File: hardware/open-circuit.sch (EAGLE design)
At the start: 72 parts, among them IC1 PIC16F1825SO14, IC2 74HC595D, IC3 MCP4728_QUAD_DAC, IC4 LM324D, IC6 LM27675M5_CHARGEPUMP

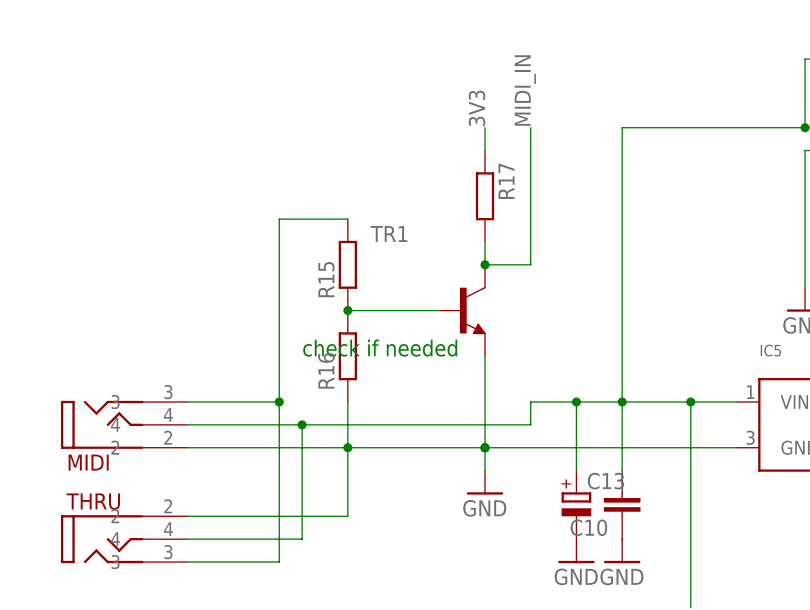
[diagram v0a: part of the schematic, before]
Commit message: fix input transistor
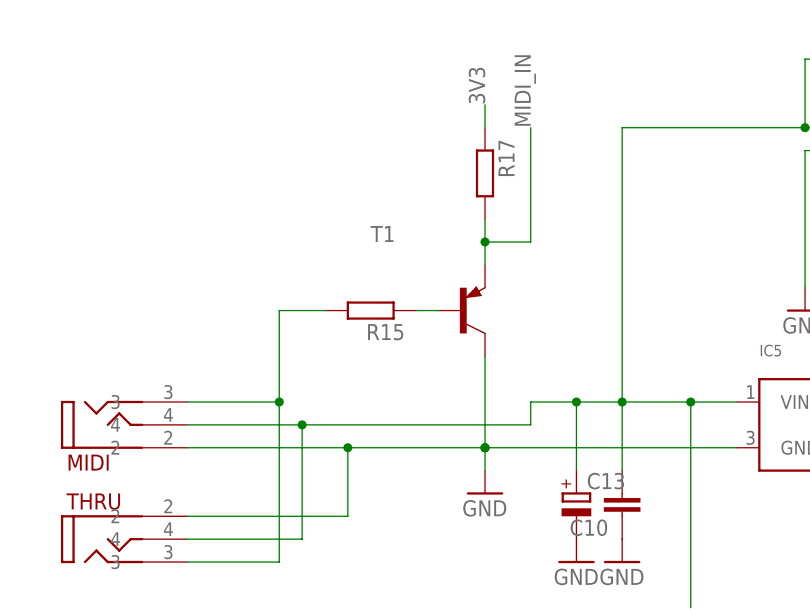
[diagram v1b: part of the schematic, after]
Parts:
- removed R16: (no value), rcl:R-EU_R0805
- removed TR1: (no value), transistor:MMBT3904LT1-NPN-SOT23-BEC
- added T1: (no value), transistor:MMBT3906LT1-PNP-SOT23-BEC
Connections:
- removed net N$19: R15.1, R16.2, TR1.B
- new net N$14: R15.1, T1.B
- net GND: now also T1.C; no longer R16.1, TR1.E
- net MIDI_IN: now also T1.E; no longer TR1.C
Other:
- note removed: "check if needed"
- moved on the sheet: R15, R17
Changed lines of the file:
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@@
 <part name="GND2" library="supply1" deviceset="GND" device=""/>
 <part name="IC5" library="microbuilder" deviceset="VREG_SOT23" device=""/>
-<part name="TR1" library="transistor" deviceset="*-NPN-" device="SOT23-BEC" technology="MMBT3904LT1"/>
-<part name="R16" library="rcl" deviceset="R-EU_" device="R0805"/>
 <part name="R17" library="rcl" deviceset="R-EU_" device="R0805"/>
 <part name="C10" library="rcl" deviceset="C-EU" device="C0805"/>
@@
 <part name="GND23" library="supply1" deviceset="GND" device=""/>
 <part name="SW1" library="switch-omron" deviceset="31-XX" device=""/>
+<part name="T1" library="transistor" deviceset="*-PNP-" device="SOT23-BEC" technology="MMBT3906LT1"/>
 </parts>
 <sheets>
 <sheet>
 <plain>
-<text x="-66.04" y="144.78" size="1.778" layer="91">check if needed</text>
 </plain>
 <instances>
@@
 <instance part="GND2" gate="1" x="116.84" y="-27.94"/>
 <instance part="IC5" gate="G$1" x="-7.62" y="137.16"/>
-<instance part="TR1" gate="G$1" x="-48.26" y="149.86"/>
-<instance part="R16" gate="G$1" x="-60.96" y="144.78" rot="R90"/>
-<instance part="R17" gate="G$1" x="-45.72" y="162.56" rot="R270"/>
+<instance part="R17" gate="G$1" x="-45.72" y="165.1" rot="R270"/>
 <instance part="C10" gate="G$1" x="-30.48" y="127" rot="R180"/>
 <instance part="GND3" gate="1" x="-45.72" y="129.54"/>
@@
 <instance part="GND6" gate="1" x="-35.56" y="121.92"/>
 <instance part="GND7" gate="1" x="-30.48" y="121.92"/>
-<instance part="R15" gate="G$1" x="-60.96" y="154.94" rot="R90"/>
+<instance part="R15" gate="G$1" x="-58.42" y="149.86" rot="R180"/>
 <instance part="IC6" gate="G$1" x="7.62" y="167.64"/>
 <instance part="C15" gate="G$1" x="30.48" y="160.02"/>
@@
 <instance part="GND23" gate="1" x="-15.24" y="-5.08"/>
 <instance part="SW1" gate="1" x="-68.58" y="17.78" rot="MR270"/>
+<instance part="T1" gate="G$1" x="-48.26" y="149.86"/>
 </instances>
 <busses>
@@
 <pinref part="IC5" gate="G$1" pin="GND"/>
 <wire x1="-78.74" y1="134.62" x2="-60.96" y2="134.62" width="0.1524" layer="91"/>
-<pinref part="TR1" gate="G$1" pin="E"/>
 <wire x1="-60.96" y1="134.62" x2="-45.72" y2="134.62" width="0.1524" layer="91"/>
 <wire x1="-45.72" y1="134.62" x2="-17.78" y2="134.62" width="0.1524" layer="91"/>
-<wire x1="-45.72" y1="144.78" x2="-45.72" y2="134.62" width="0.1524" layer="91"/>
 <junction x="-45.72" y="134.62"/>
 <junction x="-45.72" y="134.62"/>
 <pinref part="GND3" gate="1" pin="GND"/>
 <wire x1="-45.72" y1="132.08" x2="-45.72" y2="134.62" width="0.1524" layer="91"/>
-<pinref part="R16" gate="G$1" pin="1"/>
-<wire x1="-60.96" y1="139.7" x2="-60.96" y2="134.62" width="0.1524" layer="91"/>
 <junction x="-60.96" y="134.62"/>
 <pinref part="THRU" gate="G$1" pin="2"/>
 <wire x1="-78.74" y1="127" x2="-60.96" y2="127" width="0.1524" layer="91"/>
 <wire x1="-60.96" y1="127" x2="-60.96" y2="134.62" width="0.1524" layer="91"/>
+<pinref part="T1" gate="G$1" pin="C"/>
+<wire x1="-45.72" y1="144.78" x2="-45.72" y2="134.62" width="0.1524" layer="91"/>
 </segment>
 <segment>
@@
 <net name="MIDI_IN" class="0">
 <segment>
-<pinref part="TR1" gate="G$1" pin="C"/>
+<label x="-40.64" y="170.18" size="1.778" layer="95" rot="R90"/>
+<pinref part="T1" gate="G$1" pin="E"/>
 <pinref part="R17" gate="G$1" pin="2"/>
+<wire x1="-40.64" y1="157.48" x2="-40.64" y2="170.18" width="0.1524" layer="91"/>
 <wire x1="-45.72" y1="154.94" x2="-45.72" y2="157.48" width="0.1524" layer="91"/>
-<wire x1="-45.72" y1="154.94" x2="-40.64" y2="154.94" width="0.1524" layer="91"/>
-<junction x="-45.72" y="154.94"/>
-<label x="-40.64" y="170.18" size="1.778" layer="95" rot="R90"/>
-<wire x1="-40.64" y1="154.94" x2="-40.64" y2="170.18" width="0.1524" layer="91"/>
+<wire x1="-45.72" y1="157.48" x2="-45.72" y2="160.02" width="0.1524" layer="91"/>
+<wire x1="-45.72" y1="157.48" x2="-40.64" y2="157.48" width="0.1524" layer="91"/>
+<junction x="-45.72" y="157.48"/>
 </segment>
 <segment>
@@
 <segment>
 <pinref part="R17" gate="G$1" pin="1"/>
-<wire x1="-45.72" y1="167.64" x2="-45.72" y2="170.18" width="0.1524" layer="91"/>
-<label x="-45.72" y="170.18" size="1.778" layer="95" rot="R90"/>
+<wire x1="-45.72" y1="170.18" x2="-45.72" y2="172.72" width="0.1524" layer="91"/>
+<label x="-45.72" y="172.72" size="1.778" layer="95" rot="R90"/>
 </segment>
 <segment>
@@
 </segment>
 </net>
-<net name="N$19" class="0">
-<segment>
-<pinref part="R16" gate="G$1" pin="2"/>
-<pinref part="R15" gate="G$1" pin="1"/>
-<pinref part="TR1" gate="G$1" pin="B"/>
-<wire x1="-60.96" y1="149.86" x2="-50.8" y2="149.86" width="0.1524" layer="91"/>
-<junction x="-60.96" y="149.86"/>
-</segment>
-</net>
 <net name="N$20" class="0">
 <segment>
 <pinref part="MIDI" gate="G$1" pin="3"/>
 <wire x1="-78.74" y1="139.7" x2="-68.58" y2="139.7" width="0.1524" layer="91"/>
-<wire x1="-68.58" y1="139.7" x2="-68.58" y2="160.02" width="0.1524" layer="91"/>
-<pinref part="R15" gate="G$1" pin="2"/>
-<wire x1="-68.58" y1="160.02" x2="-60.96" y2="160.02" width="0.1524" layer="91"/>
+<wire x1="-68.58" y1="139.7" x2="-68.58" y2="149.86" width="0.1524" layer="91"/>
 <pinref part="THRU" gate="G$1" pin="3"/>
 <wire x1="-78.74" y1="121.92" x2="-68.58" y2="121.92" width="0.1524" layer="91"/>
 <wire x1="-68.58" y1="121.92" x2="-68.58" y2="139.7" width="0.1524" layer="91"/>
 <junction x="-68.58" y="139.7"/>
+<pinref part="R15" gate="G$1" pin="2"/>
+<wire x1="-63.5" y1="149.86" x2="-68.58" y2="149.86" width="0.1524" layer="91"/>
 </segment>
 </net>
@@
 </segment>
 </net>
+<net name="N$14" class="0">
+<segment>
+<pinref part="R15" gate="G$1" pin="1"/>
+<pinref part="T1" gate="G$1" pin="B"/>
+<wire x1="-53.34" y1="149.86" x2="-50.8" y2="149.86" width="0.1524" layer="91"/>
+</segment>
+</net>

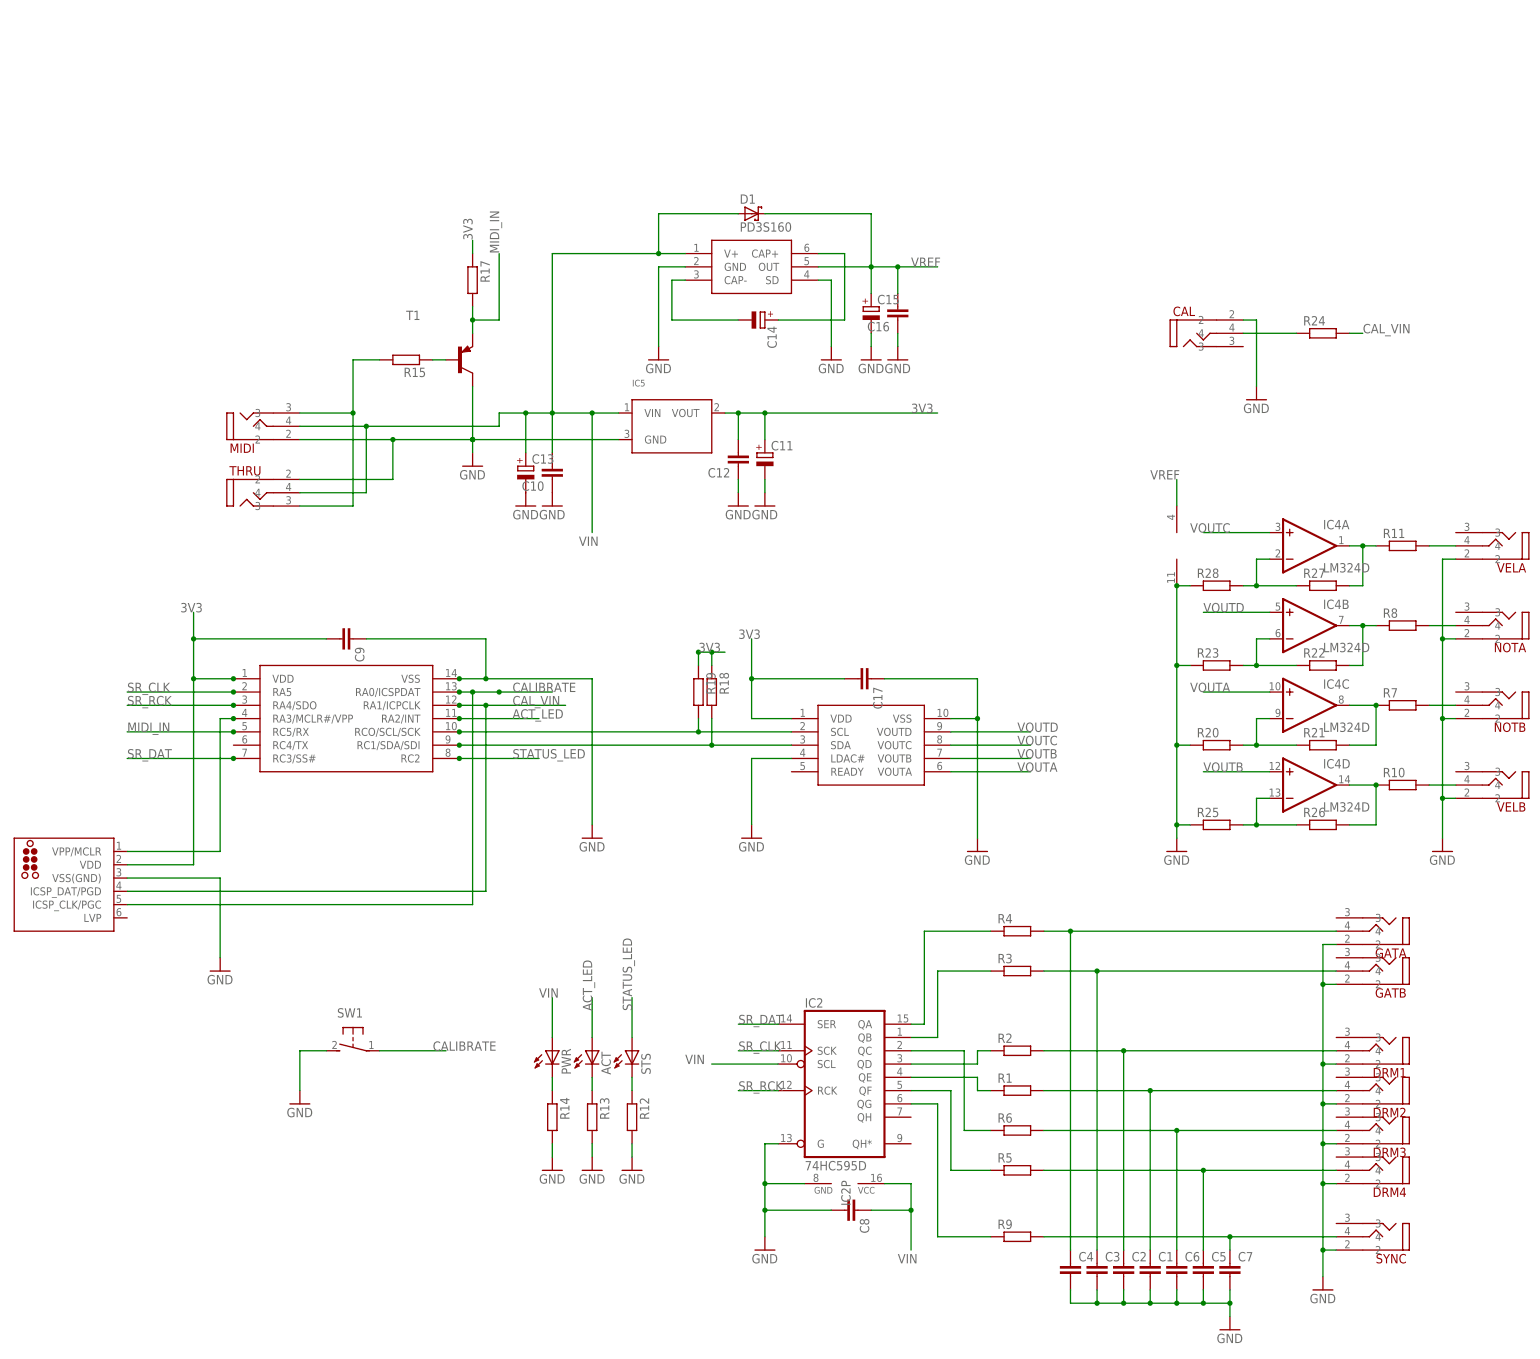
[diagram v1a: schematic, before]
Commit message: add 5V voltage reg
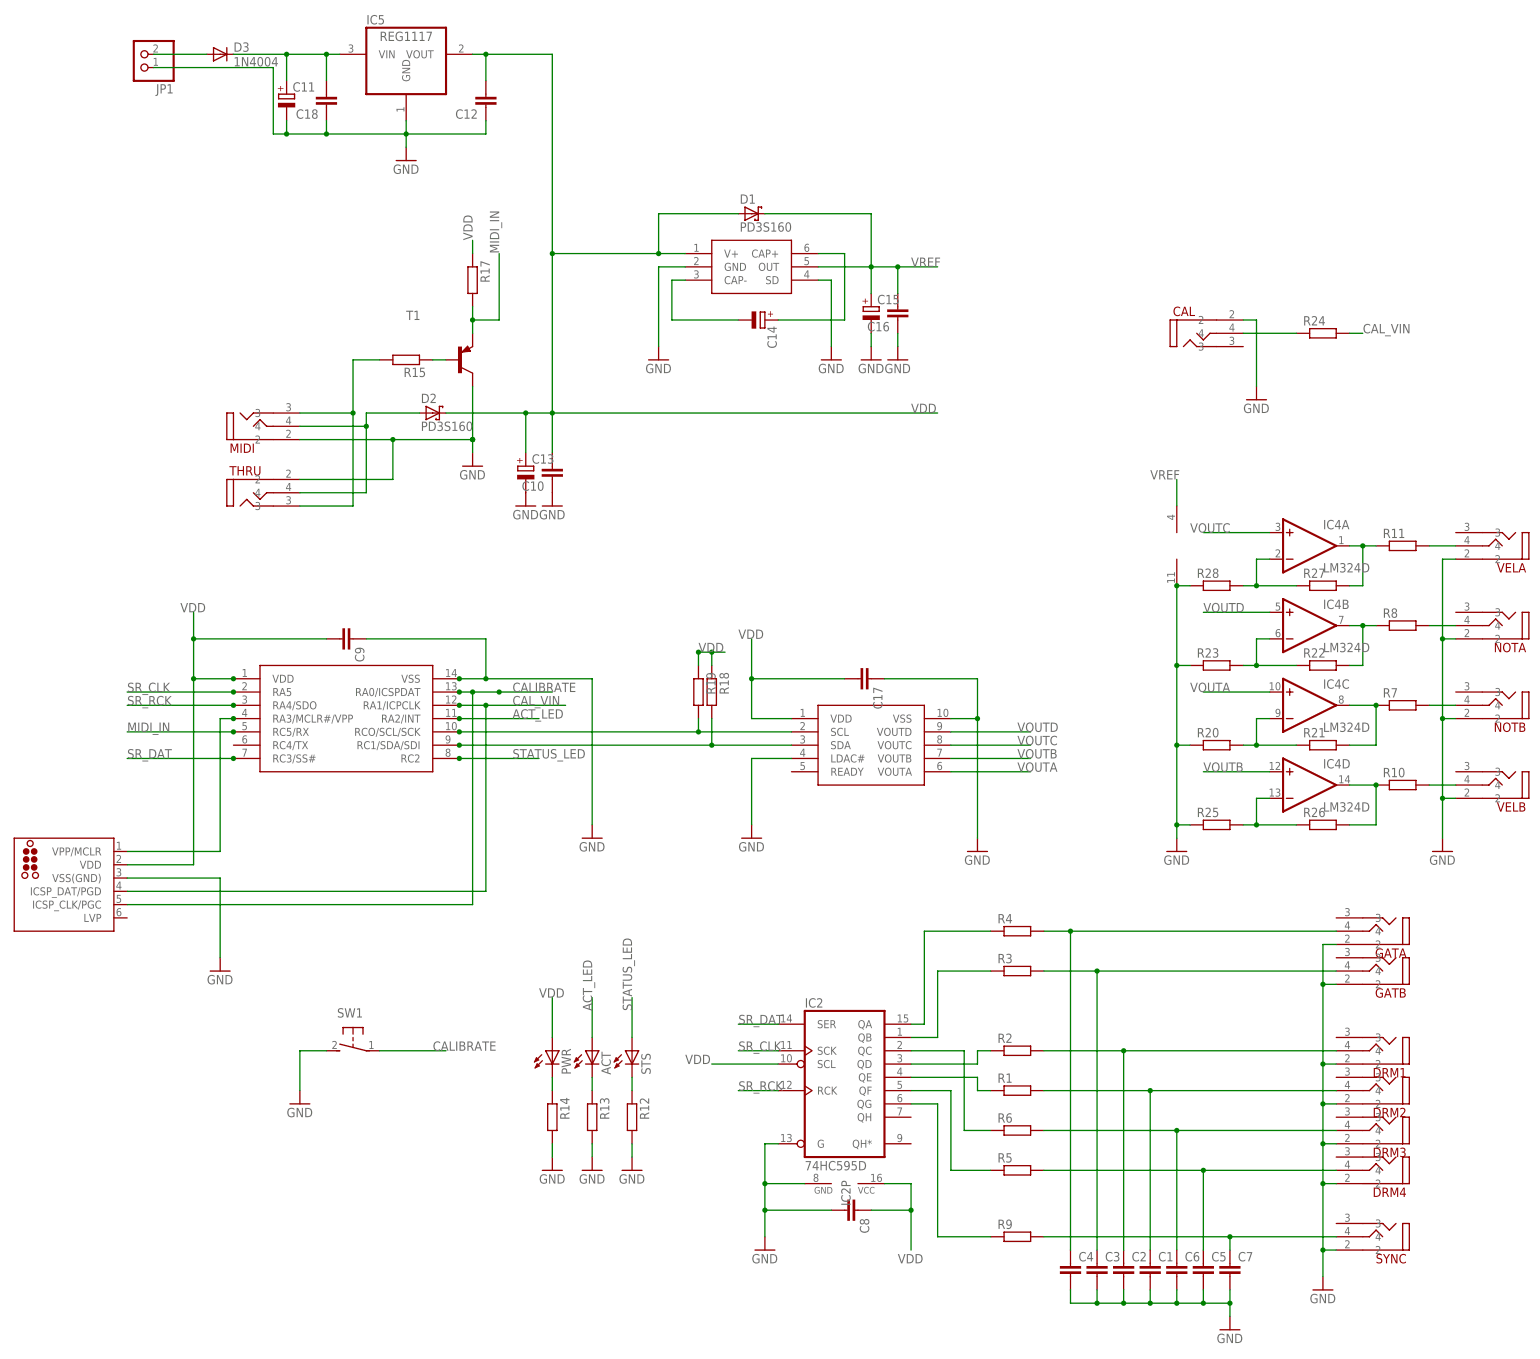
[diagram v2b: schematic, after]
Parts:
- added C18: (no value), rcl:C-EUC0805
- added D2: PD3S160, diode:PD3S160
- added D3: 1N4004, jasons_stuff:1N4004
- added JP1: (no value), pinhead:PINHD-1X2
- C11: device rcl:CPOL-EUSMCA -> resistor:CPOL-EUE2.5-5
- IC5: value (none) -> REG1117; device microbuilder:VREG_SOT23 -> burr-brown:REG1117
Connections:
- removed net 3V3: C11.+, C12.2, C17.2, C9.2, IC1.VDD, IC3.VDD, IC5.VOUT, ISCP.VDD, R17.1, R18.1, R19.1
- removed net VIN: C10.2, C13.+, C8.1, D1.A, IC2A.SCL, IC2P.VCC, IC5.VIN, IC6.V+, MIDI.4, PWR.A, THRU.4
- new net N$19: C11.+, C18.2, D3.C, IC5.VIN
- new net N$39: D2.A, MIDI.4, THRU.4
- new net N$40: D3.A, JP1.2
- new net VDD: C10.2, C12.2, C13.+, C17.2, C8.1, C9.2, D1.A, D2.C, IC1.VDD, IC2A.SCL, IC2P.VCC, IC3.VDD, IC5.VOUT, IC6.V+, ISCP.VDD, PWR.A, R17.1, R18.1, R19.1
- net GND: now also C18.1, JP1.1
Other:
- moved on the sheet: C11, C12, IC5

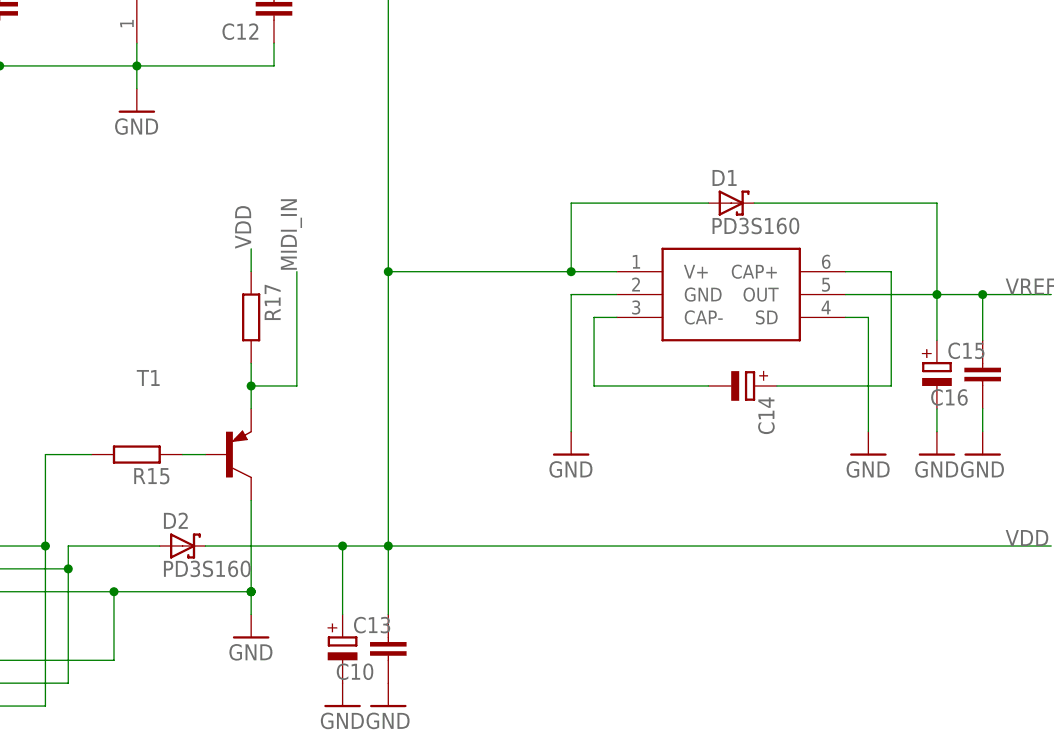
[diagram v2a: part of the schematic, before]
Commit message: change schottky footprint
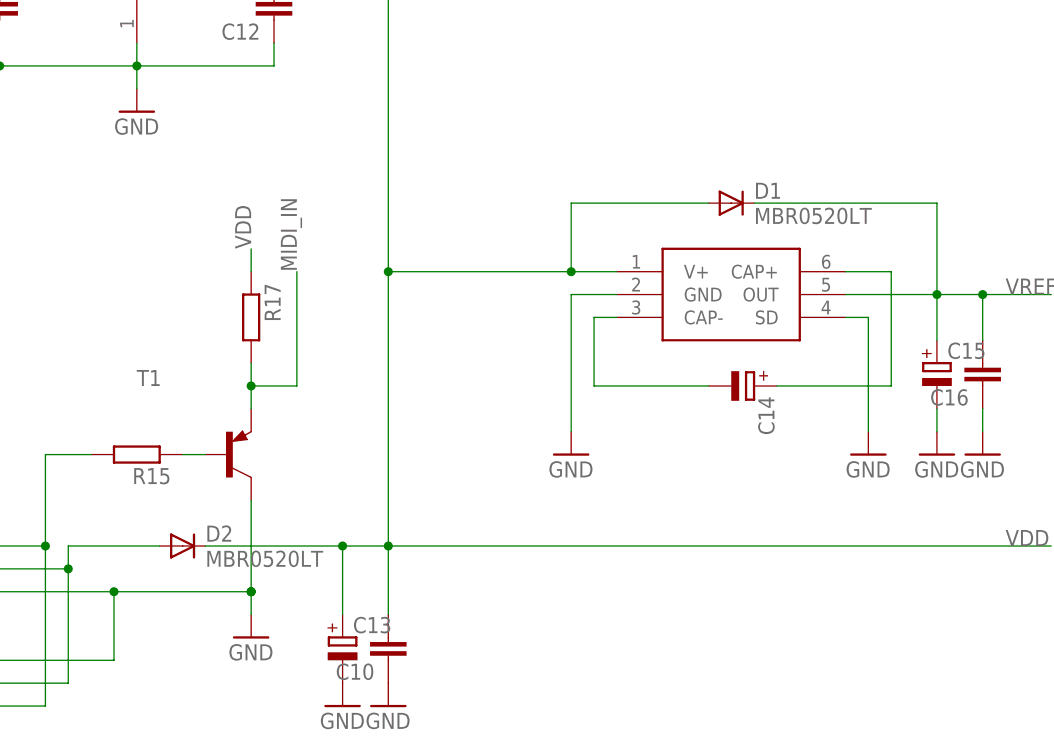
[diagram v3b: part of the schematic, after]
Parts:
- D1, D2: value PD3S160 -> MBR0520LT; device diode:PD3S160 -> diode:MBR0520LT
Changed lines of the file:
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@@
 <part name="GND10" library="supply1" deviceset="GND" device=""/>
 <part name="GND11" library="supply1" deviceset="GND" device=""/>
-<part name="D1" library="diode" deviceset="PD3S160" device=""/>
+<part name="D1" library="diode" deviceset="MBR0520LT" device=""/>
 <part name="R19" library="rcl" deviceset="R-EU_" device="R0805"/>
 <part name="R18" library="rcl" deviceset="R-EU_" device="R0805"/>
@@
 <part name="C11" library="resistor" deviceset="CPOL-EU" device="E2.5-5"/>
 <part name="C18" library="rcl" deviceset="C-EU" device="C0805"/>
-<part name="D2" library="diode" deviceset="PD3S160" device=""/>
+<part name="D2" library="diode" deviceset="MBR0520LT" device=""/>
 <part name="C12" library="rcl" deviceset="C-EU" device="C0805"/>
 <part name="D3" library="jasons_stuff" deviceset="1N4004" device=""/>
